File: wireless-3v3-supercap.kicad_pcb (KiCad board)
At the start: 2 copper layers, 85 x 40 mm, 6 parts, among them J1 POWER-OUT, J2 POWER-IN, U1 BQ33100PWR

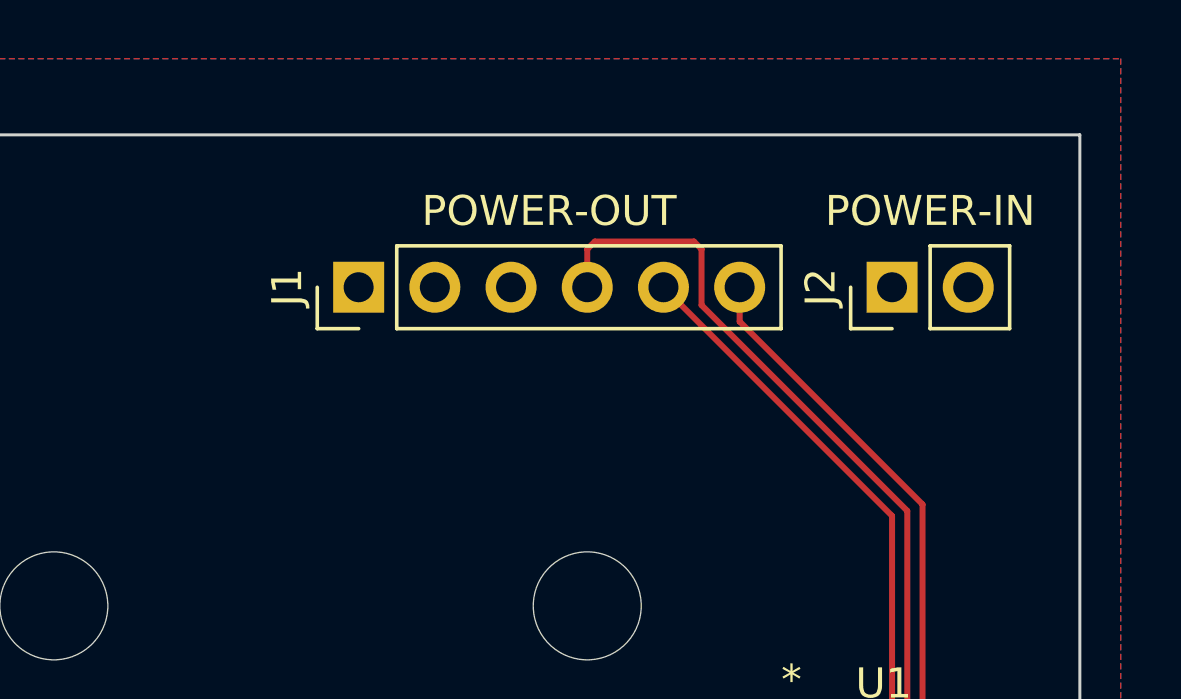
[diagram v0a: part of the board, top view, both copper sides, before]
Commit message: Move pin headers further away from the edge of the PCB
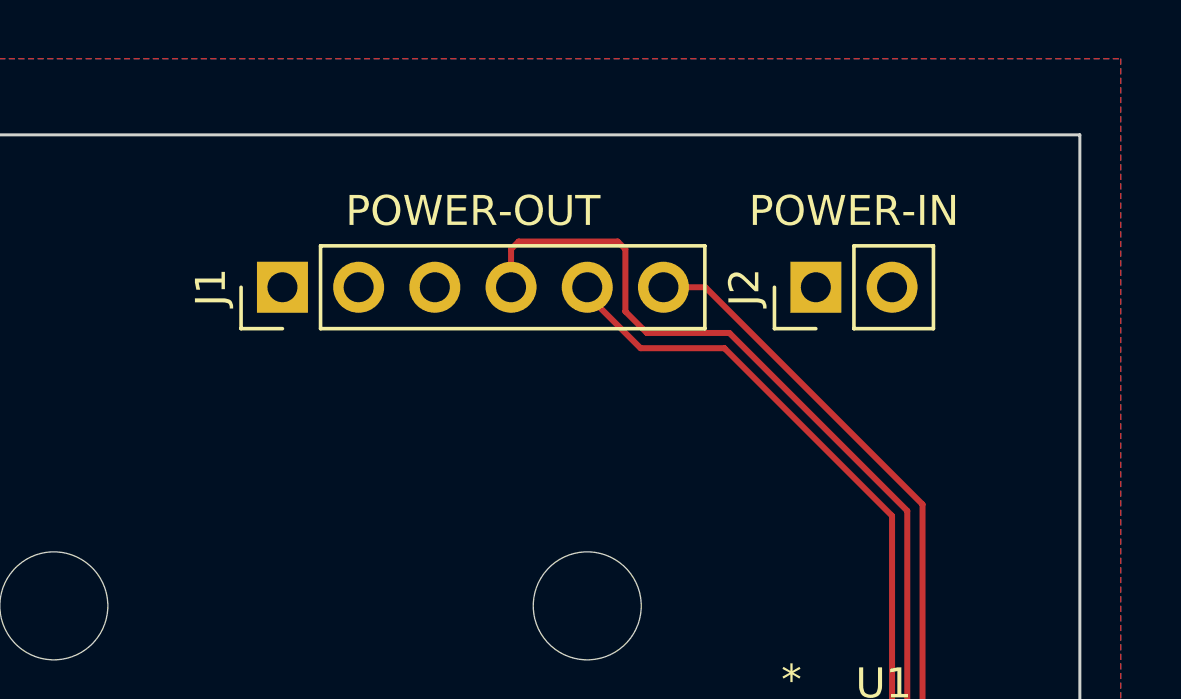
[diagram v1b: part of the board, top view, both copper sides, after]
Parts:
- moved J1 2.54 mm to (83.8, 30.5)
- moved J2 2.54 mm to (101.6, 30.5)
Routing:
- net SDA: track 25.9 -> 28.6 mm
- net FAULT: track 31.3 -> 34.0 mm
- net SCL: track 23.6 -> 25.4 mm
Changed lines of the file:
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@@
 	(footprint "Connector_PinHeader_2.54mm:PinHeader_1x02_P2.54mm_Vertical"
 		(layer "F.Cu")
-		(at 104.14 30.48 90)
+		(at 101.6 30.48 90)
 		(descr "Through hole straight pin header, 1x02, 2.54mm pitch, single row")
 		(tags "Through hole pin header THT 1x02 2.54mm single row")
@@
 	(footprint "Connector_PinHeader_2.54mm:PinHeader_1x06_P2.54mm_Vertical"
 		(layer "F.Cu")
-		(at 86.36 30.48 90)
+		(at 83.82 30.48 90)
 		(descr "Through hole straight pin header, 1x06, 2.54mm pitch, single row")
 		(tags "Through hole pin header THT 1x06 2.54mm single row")
@@
 		(layer "Cmts.User")
 		(pts
-			(xy 25.4 65.4) (xy 110.4 65.4)
+			(xy 107.696 48.006) (xy 110.4 47.860499)
 		)
-		(height 5.72)
+		(height -5.08)
 		(orientation 0)
 		(format
 			(prefix "")
 			(suffix "")
-			(units 3)
+			(units 2)
 			(units_format 1)
 			(precision 4)
@@
 			(keep_text_aligned yes)
 		)
-		(gr_text "85 mm"
-			(at 67.9 69.97 0)
+		(gr_text "2.704 mm"
+			(at 109.048 41.826 0)
 			(layer "Cmts.User")
 			(effects
 				(font
 					(size 1 1)
-					(thickness 0.15)
+					(thickness 0.1)
 				)
 			)
@@
 		(layer "Cmts.User")
 		(pts
-			(xy 104.775 53.975) (xy 110.4 53.975)
+			(xy 25.4 65.4) (xy 110.4 65.4)
 		)
-		(height 4.445)
+		(height 5.72)
 		(orientation 0)
 		(format
@@
 			(suffix "")
 			(units 3)
-			(units_format 0)
+			(units_format 1)
 			(precision 4)
 			(suppress_zeroes yes)
@@
 			(keep_text_aligned yes)
 		)
-		(gr_text "5.625"
-			(at 107.5875 57.27 0)
+		(gr_text "85 mm"
+			(at 67.9 69.97 0)
 			(layer "Cmts.User")
 			(effects
@@
 		(layer "Cmts.User")
 		(pts
-			(xy 99.17 30.48) (xy 110.4 30.48)
+			(xy 105.52 30.48) (xy 110.4 30.48)
 		)
 		(height -10.16)
@@
 			(keep_text_aligned yes)
 		)
-		(gr_text "11.23 mm"
-			(at 104.785 19.17 0)
+		(gr_text "4.88 mm"
+			(at 107.96 19.17 0)
 			(layer "Cmts.User")
 			(effects
@@
 	)
 	(segment
-		(start 96.52 30.48)
+		(start 98.552 32.512)
 		(end 104.14 38.1)
 		(width 0.2)
@@
 	)
 	(segment
-		(start 104.14 50.068198)
-		(end 105.6418 51.569998)
+		(start 93.98 30.48)
+		(end 93.98 30.734)
 		(width 0.2)
 		(layer "F.Cu")
@@
 	)
 	(segment
-		(start 105.6418 50.269999)
-		(end 106.68 50.269999)
+		(start 93.98 30.734)
+		(end 95.758 32.512)
 		(width 0.2)
 		(layer "F.Cu")
-		(net 8)
+		(net 6)
 	)
 	(segment
-		(start 105.156 37.719)
-		(end 105.156 49.784199)
+		(start 104.14 50.068198)
+		(end 105.6418 51.569998)
+		(width 0.2)
+		(layer "F.Cu")
+		(net 6)
+	)
+	(segment
+		(start 95.758 32.512)
+		(end 98.552 32.512)
+		(width 0.2)
+		(layer "F.Cu")
+		(net 6)
+	)
+	(segment
+		(start 96.52 30.48)
+		(end 97.917 30.48)
 		(width 0.2)
 		(layer "F.Cu")
@@
 	)
 	(segment
-		(start 99.06 31.623)
+		(start 97.917 30.48)
 		(end 105.156 37.719)
 		(width 0.2)
@@
 	)
 	(segment
-		(start 99.06 30.48)
-		(end 99.06 31.623)
+		(start 105.6418 50.269999)
+		(end 106.68 50.269999)
+		(width 0.2)
+		(layer "F.Cu")
+		(net 8)
+	)
+	(segment
+		(start 105.156 37.719)
+		(end 105.156 49.784199)
 		(width 0.2)
 		(layer "F.Cu")
@@
 	)
 	(segment
-		(start 104.648 49.926197)
-		(end 105.6418 50.919997)
+		(start 95.25 29.21)
+		(end 95.25 31.28588)
 		(width 0.2)
 		(layer "F.Cu")
@@
 	)
 	(segment
-		(start 93.98 30.48)
-		(end 93.98 29.21)
+		(start 98.71824 32.004)
+		(end 104.648 37.93376)
+		(width 0.2)
+		(layer "F.Cu")
+		(net 26)
+	)
+	(segment
+		(start 94.996 28.956)
+		(end 95.25 29.21)
 		(width 0.2)
 		(layer "F.Cu")
@@
 	)
 	(segment
-		(start 97.79 29.21)
-		(end 97.79 31.07576)
+		(start 104.648 37.93376)
+		(end 104.648 49.926197)
 		(width 0.2)
 		(layer "F.Cu")
@@
 	)
 	(segment
-		(start 97.536 28.956)
-		(end 97.79 29.21)
+		(start 95.25 31.28588)
+		(end 95.96812 32.004)
 		(width 0.2)
 		(layer "F.Cu")
@@
 	)
 	(segment
-		(start 94.234 28.956)
-		(end 97.536 28.956)
+		(start 105.6418 50.919997)
+		(end 106.68 50.919997)
 		(width 0.2)
 		(layer "F.Cu")
@@
 	)
 	(segment
-		(start 93.98 29.21)
-		(end 94.234 28.956)
+		(start 95.96812 32.004)
+		(end 98.71824 32.004)
 		(width 0.2)
 		(layer "F.Cu")
@@
 	)
 	(segment
-		(start 97.79 31.07576)
-		(end 104.648 37.93376)
+		(start 91.694 28.956)
+		(end 94.996 28.956)
 		(width 0.2)
 		(layer "F.Cu")
@@
 	)
 	(segment
-		(start 104.648 37.93376)
-		(end 104.648 49.926197)
+		(start 91.44 30.48)
+		(end 91.44 29.21)
 		(width 0.2)
 		(layer "F.Cu")
@@
 	)
 	(segment
-		(start 105.6418 50.919997)
-		(end 106.68 50.919997)
+		(start 91.44 29.21)
+		(end 91.694 28.956)
+		(width 0.2)
+		(layer "F.Cu")
+		(net 26)
+	)
+	(segment
+		(start 104.648 49.926197)
+		(end 105.6418 50.919997)
 		(width 0.2)
 		(layer "F.Cu")

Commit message: Make discharge tracks thicker
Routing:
- net Net-(U1-VCCPACK): track 79.9 -> 67.4 mm
- net Net-(SW1-C): track 100.2 -> 101.1 mm
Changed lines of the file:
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@@
 			(layers "*.Cu" "*.Mask")
 			(remove_unused_layers no)
-			(clearance 2)
 		)
 		(pad "" thru_hole circle
@@
 			(layers "*.Cu" "*.Mask")
 			(remove_unused_layers no)
-			(clearance 2)
 		)
 		(pad "1" thru_hole roundrect
@@
 	)
 	(segment
-		(start 80.01 46.355)
-		(end 33.02 46.355)
-		(width 1)
+		(start 81.28 46.355)
+		(end 91.44 56.515)
+		(width 2)
 		(layer "B.Cu")
 		(net 4)
 	)
 	(segment
-		(start 99.43 58.79)
-		(end 99.43 60.96)
-		(width 1)
+		(start 33.02 46.355)
+		(end 81.28 46.355)
+		(width 2)
 		(layer "B.Cu")
 		(net 4)
 	)
 	(segment
-		(start 81.65 60.96)
-		(end 81.65 58.685)
-		(width 1)
+		(start 81.65 58.685)
+		(end 83.82 56.515)
+		(width 2)
 		(layer "B.Cu")
 		(net 4)
 	)
 	(segment
-		(start 33.02 46.355)
-		(end 30.48 43.815)
-		(width 1)
+		(start 97.155 56.515)
+		(end 99.43 58.79)
+		(width 2)
 		(layer "B.Cu")
 		(net 4)
 	)
 	(segment
-		(start 30.48 43.815)
-		(end 30.48 33.02)
-		(width 1)
+		(start 30.48 33.02)
+		(end 30.48 43.815)
+		(width 2)
 		(layer "B.Cu")
 		(net 4)
 	)
 	(segment
-		(start 97.79 57.15)
-		(end 99.43 58.79)
-		(width 1)
+		(start 30.48 43.815)
+		(end 33.02 46.355)
+		(width 2)
 		(layer "B.Cu")
 		(net 4)
 	)
 	(segment
-		(start 81.65 58.685)
-		(end 83.185 57.15)
-		(width 1)
+		(start 91.44 56.515)
+		(end 97.155 56.515)
+		(width 2)
 		(layer "B.Cu")
 		(net 4)
 	)
 	(segment
-		(start 83.185 57.15)
-		(end 90.805 57.15)
-		(width 1)
+		(start 81.65 60.96)
+		(end 81.65 58.685)
+		(width 2)
 		(layer "B.Cu")
 		(net 4)
 	)
 	(segment
-		(start 90.805 57.15)
-		(end 97.79 57.15)
-		(width 1)
+		(start 83.82 56.515)
+		(end 91.44 56.515)
+		(width 2)
 		(layer "B.Cu")
 		(net 4)
 	)
 	(segment
-		(start 90.805 57.15)
-		(end 80.01 46.355)
-		(width 1)
+		(start 99.43 58.79)
+		(end 99.43 60.96)
+		(width 2)
 		(layer "B.Cu")
 		(net 4)
@@
 	)
 	(segment
-		(start 90.424 60.96)
-		(end 88.53 60.96)
-		(width 0.5)
+		(start 70.75 60.96)
+		(end 70.75 58.685)
+		(width 2)
 		(layer "F.Cu")
 		(net 25)
 	)
 	(segment
-		(start 88.53 58.685)
-		(end 86.995 57.15)
-		(width 1)
+		(start 90.424 60.96)
+		(end 88.53 60.96)
+		(width 0.5)
 		(layer "F.Cu")
 		(net 25)
 	)
 	(segment
-		(start 86.995 57.15)
-		(end 54.63 57.15)
-		(width 1)
+		(start 86.36 56.515)
+		(end 68.58 56.515)
+		(width 2)
 		(layer "F.Cu")
 		(net 25)
 	)
 	(segment
-		(start 54.63 57.15)
-		(end 53.467 58.313)
-		(width 1)
+		(start 68.58 56.515)
+		(end 55.265 56.515)
+		(width 2)
 		(layer "F.Cu")
 		(net 25)
@@
 	)
 	(segment
-		(start 88.53 60.96)
-		(end 88.53 58.685)
-		(width 1)
+		(start 70.75 58.685)
+		(end 68.58 56.515)
+		(width 2)
 		(layer "F.Cu")
 		(net 25)
@@
 	)
 	(segment
-		(start 99.456001 45.069999)
-		(end 92.202 52.324)
-		(width 0.5)
+		(start 88.53 58.685)
+		(end 86.36 56.515)
+		(width 2)
 		(layer "F.Cu")
 		(net 25)
 	)
 	(segment
-		(start 56.114 60.96)
+		(start 55.265 56.515)
 		(end 53.467 58.313)
-		(width 1)
-		(layer "B.Cu")
+		(width 2)
+		(layer "F.Cu")
 		(net 25)
 	)
 	(segment
-		(start 70.75 60.96)
-		(end 56.114 60.96)
-		(width 1)
-		(layer "B.Cu")
+		(start 99.456001 45.069999)
+		(end 92.202 52.324)
+		(width 0.5)
+		(layer "F.Cu")
+		(net 25)
+	)
+	(segment
+		(start 88.53 60.96)
+		(end 88.53 58.685)
+		(width 2)
+		(layer "F.Cu")
 		(net 25)
 	)

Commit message: Remove BQ33100PWR and discharge resistors
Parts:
- removed R1, R2: 900-910mΩ 1% 20-100W, Package_TO_SOT_THT:TO-247-2_Horizontal_TabDown
- removed U1: BQ33100PWR, BQ33100PWR:PW24
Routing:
- net Net-(SW1-C): track 101.1 -> 0.00 mm
- net Net-(SW1-3): track 67.4 -> 2.54 mm
- net FAULT: track 34.0 -> 0.00 mm
- net SDA: track 28.6 -> 0.00 mm
- net SCL: track 25.4 -> 0.00 mm
- net GND: track 6.72 -> 0.00 mm, vias 3 -> 0

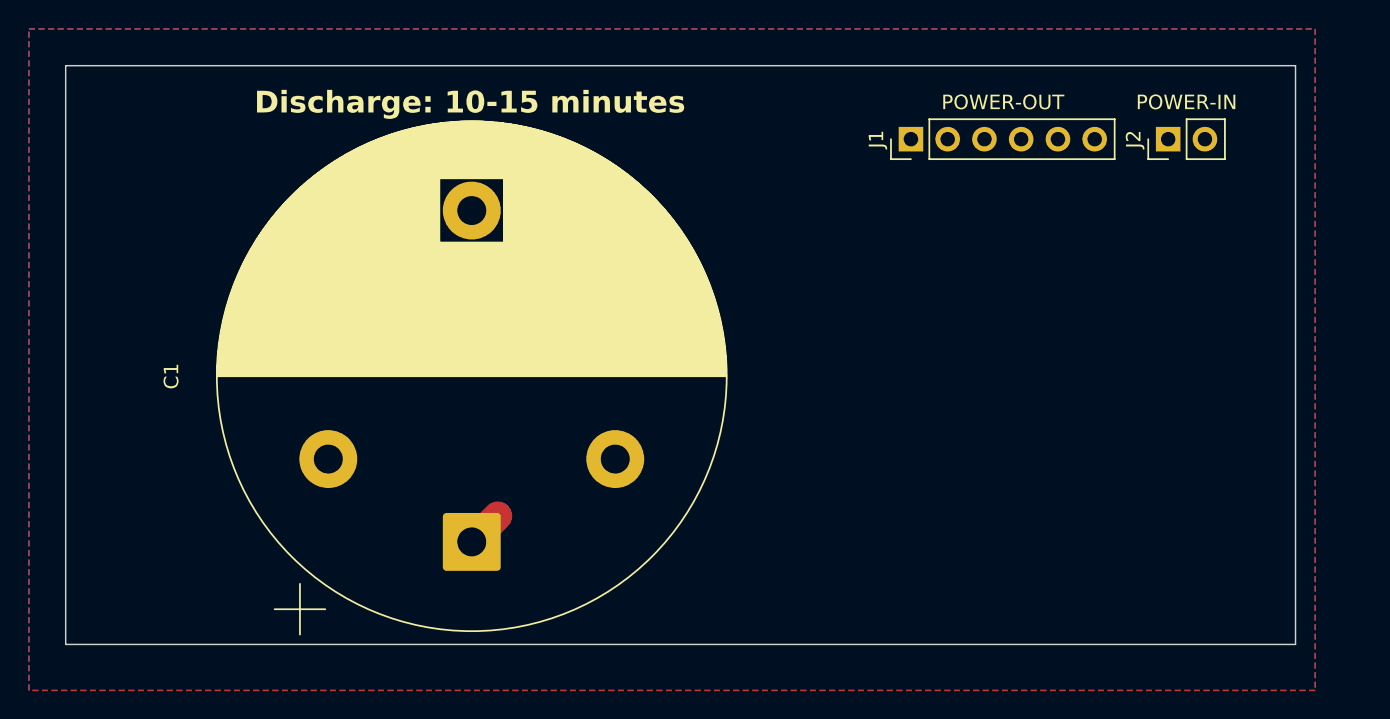
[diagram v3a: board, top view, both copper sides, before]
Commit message: Resize PCB to available space
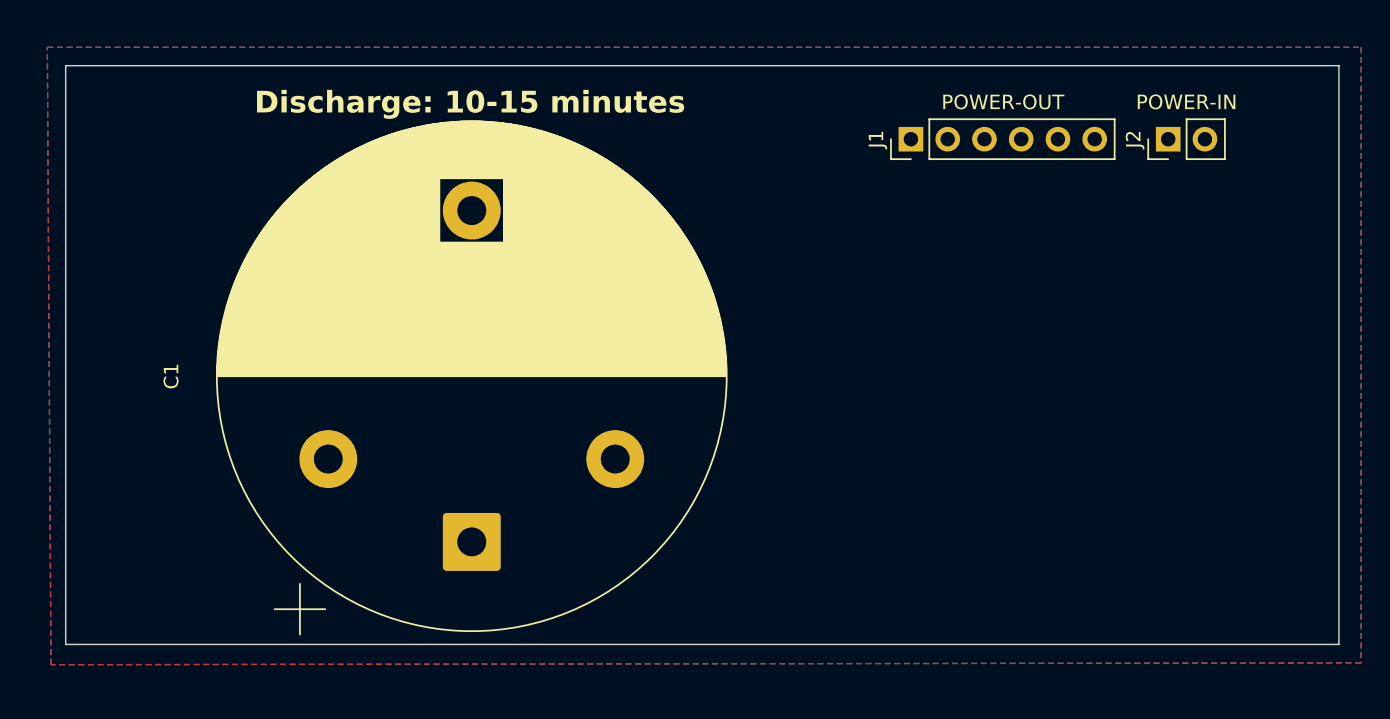
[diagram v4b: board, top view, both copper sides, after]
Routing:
- net Net-(SW1-3): track 2.54 -> 0.00 mm
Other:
- board size 85 x 40 mm -> 88 x 40 mm
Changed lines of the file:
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@@
 	(gr_rect
 		(start 25.4 25.4)
-		(end 110.4 65.4)
+		(end 113.4 65.4)
 		(stroke
 			(width 0.1)
@@
 		(layer "Cmts.User")
 		(pts
-			(xy 25.4 65.4) (xy 110.4 65.4)
+			(xy 25.4 65.4) (xy 113.4 65.4)
 		)
 		(height 5.72)
@@
 			(keep_text_aligned yes)
 		)
-		(gr_text "85 mm"
-			(at 67.9 69.97 0)
+		(gr_text "88 mm"
+			(at 69.4 69.97 0)
 			(layer "Cmts.User")
 			(effects
@@
 		(layer "Cmts.User")
 		(pts
-			(xy 25.4 46.863) (xy 35.467 46.863)
+			(xy 25.4 65.4) (xy 28.448 65.405)
 		)
-		(height -26.543)
+		(height -43.175)
 		(orientation 0)
 		(format
@@
 			(keep_text_aligned yes)
 		)
-		(gr_text "10.067 mm"
-			(at 30.4335 19.17 0)
+		(gr_text "3.048 mm"
+			(at 26.924 21.075 0)
 			(layer "Cmts.User")
 			(effects
@@
 			(xy 110 25.4) (xy 110 65.4)
 		)
-		(height 4.3)
+		(height 10.65)
 		(orientation 1)
 		(format
@@
 		)
 		(gr_text "40 mm"
-			(at 113.15 45.4 90)
+			(at 119.5 45.4 90)
 			(layer "Cmts.User")
 			(effects
@@
 		(layer "Cmts.User")
 		(pts
-			(xy 105.52 30.48) (xy 110.4 30.48)
+			(xy 110.363 65.405) (xy 113.4 65.4)
 		)
-		(height -10.16)
+		(height -43.18)
 		(orientation 0)
 		(format
@@
 			(keep_text_aligned yes)
 		)
-		(gr_text "4.88 mm"
-			(at 107.96 19.17 0)
+		(gr_text "3.037 mm"
+			(at 111.8815 21.075 0)
 			(layer "Cmts.User")
 			(effects
@@
 			)
 		)
-	)
-	(segment
-		(start 55.265 56.515)
-		(end 53.467 58.313)
-		(width 2)
-		(layer "F.Cu")
-		(net 4)
 	)
 	(zone
@@
 		(polygon
 			(pts
-				(xy 22.86 22.86) (xy 111.76 22.86) (xy 111.76 68.58) (xy 22.86 68.58)
+				(xy 24.13 24.13) (xy 114.935 24.13) (xy 114.935 66.675) (xy 24.384 66.802)
 			)
 		)

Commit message: Add discharge circuit, and main component for charging/power out
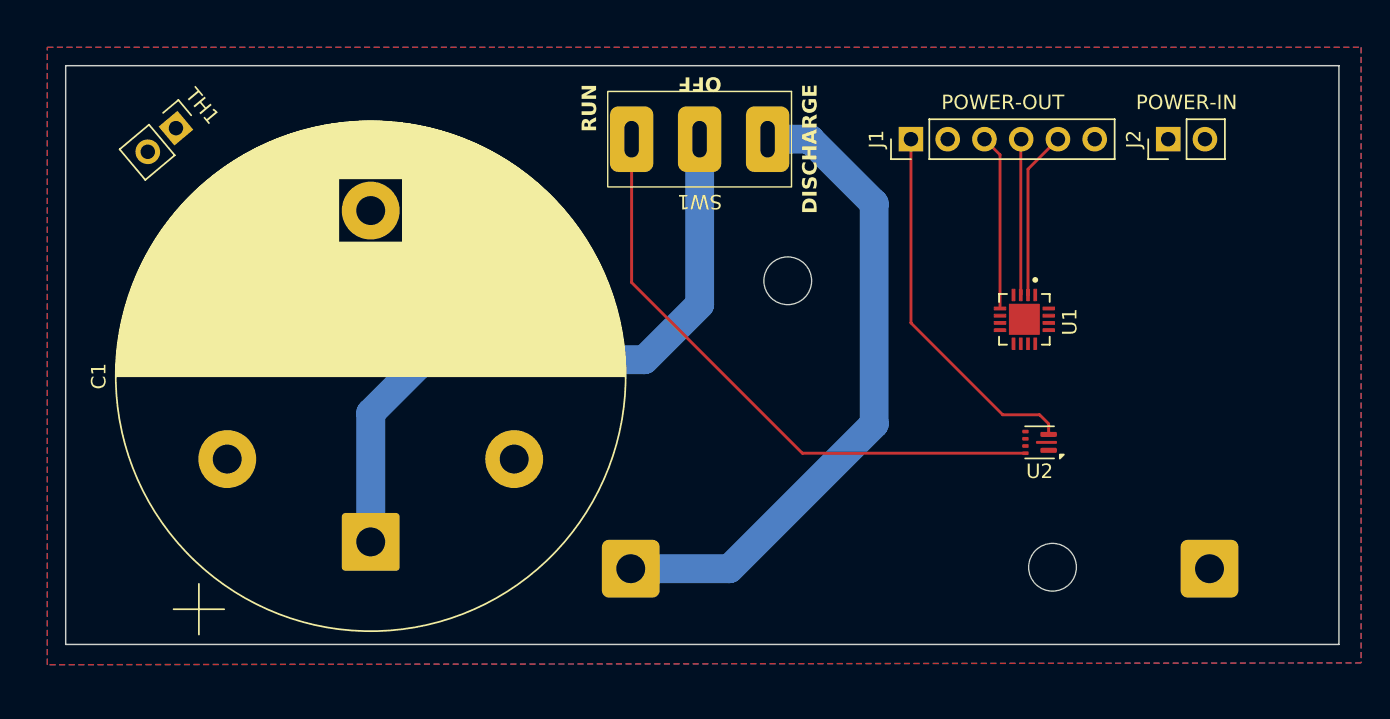
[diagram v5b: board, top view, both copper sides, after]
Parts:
- added R1: 390mΩ 5% 25W, wireless-3v3-supercap:THS25R39J, B.Cu at (84.5, 50.2)
- added SW1: MODE, wireless-3v3-supercap:E103SYZGE, F.Cu at (69.2, 30.5)
- added TH1: 10kΩ 1%, Connector_PinHeader_2.54mm:PinHeader_1x02_P2.54mm_Vertical, F.Cu at (33.0, 29.7)
- added U1: BQ24640RVAR, BQ24640RVAR:QFN50P350X350X100-17N, F.Cu at (91.7, 42.9)
- added U2: TPS61022, Package_DFN_QFN:Texas_RWU0007A_VQFN-7_2x2mm_P0.5mm, F.Cu at (92.7, 51.4)
- moved C1 6.98 mm to (46.5, 46.9)
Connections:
- net SCL renamed CAPACITOR_VOLTAGE
- C1 pad 1: Net-(SW1-3) -> /SUPERCAP
- J1 pad 3: CHARGING -> EXTERNAL_POWER_PRESENT
- J1 pad 4: FAULT -> CHARGE_STATUS
- J1 pad 5: SDA -> CHARGE_ENABLE
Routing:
- net /SUPERCAP: track 0.00 -> 46.2 mm
- net /DISCHARGE: track 0.00 -> 45.4 mm
- net /Charge/SUPERCAP: track 0.00 -> 42.0 mm
- net +3.3V: track 0.00 -> 25.8 mm
- net EXTERNAL_POWER_PRESENT: track 0.00 -> 12.1 mm
- net CHARGE_ENABLE: track 0.00 -> 11.6 mm
- net CHARGE_STATUS: track 0.00 -> 10.7 mm
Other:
- board text added: "DISCHARGE"
- board text added: "Discharge: 14-16 mins"
- board text added: "OFF"
- board text added: "RUN"
- board text removed: "Discharge: 10-15 minutes"

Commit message: Configure power output
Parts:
- added JP1: SolderJumper_2_Open, Jumper:SolderJumper-3_P1.3mm_Open_RoundedPad1.0x1.5mm_NumberLabels, F.Cu at (78.2, 51.3)
- added R3: 402kΩ 1% 125mW, Resistor_SMD:R_0805_2012Metric_Pad1.20x1.40mm_HandSolder, F.Cu at (91.7, 48.0)
- added R4: 88.7kΩ 1% 125mW, Resistor_SMD:R_0805_2012Metric_Pad1.20x1.40mm_HandSolder, F.Cu at (89.7, 48.0)
- added R5: 10kΩ 125mW, Resistor_SMD:R_0805_2012Metric_Pad1.20x1.40mm_HandSolder, F.Cu at (73.1, 53.7)
- added R6: 10kΩ 125mW, Resistor_SMD:R_0805_2012Metric_Pad1.20x1.40mm_HandSolder, F.Cu at (73.1, 48.9)
- moved U1 5.68 mm to (95.9, 39.1)
- moved SW1 0.63 mm to (69.2, 31.1)
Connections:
- U2 pad 2: unconnected-(U2-SW-Pad2) -> Net-(U2-SW)
- U2 pad 4: unconnected-(U2-FB-Pad4) -> Net-(U2-FB)
- U2 pad 5: unconnected-(U2-EN-Pad5) -> /Charge/SUPERCAP
- U2 pad 6: unconnected-(U2-MODE-Pad6) -> Net-(JP1-C)
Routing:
- net /Charge/SUPERCAP: track 42.0 -> 76.8 mm
- net +3.3V: track 25.8 -> 5.16 mm
- net Net-(JP1-C): track 0.00 -> 13.7 mm
- net Net-(JP1-B): track 0.00 -> 5.21 mm
- net Net-(JP1-A): track 0.00 -> 5.21 mm
- net CHARGE_ENABLE: track 11.6 -> 7.84 mm
- net Net-(U2-FB): track 0.00 -> 3.73 mm
- net CHARGE_STATUS: track 10.7 -> 8.66 mm
- net EXTERNAL_POWER_PRESENT: track 12.1 -> 10.6 mm
- net /SUPERCAP: track 46.2 -> 45.5 mm
- net GND: vias 0 -> 33
